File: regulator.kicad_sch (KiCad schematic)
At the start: 4 parts, among them U1 TEN20-4811WIN, U2 ADP7142AUJZ

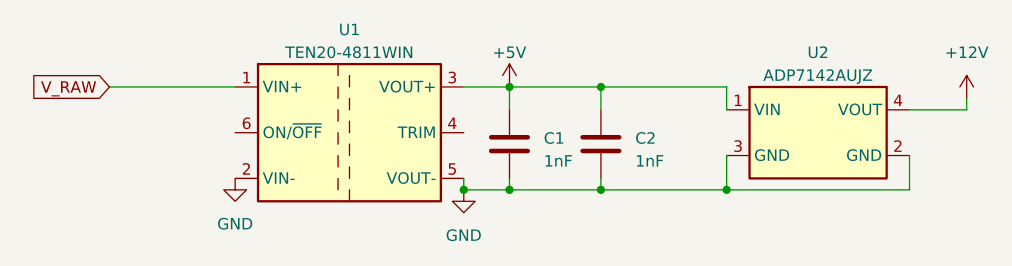
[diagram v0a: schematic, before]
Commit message: initial pcb placment, some components needs to be replaced by smd
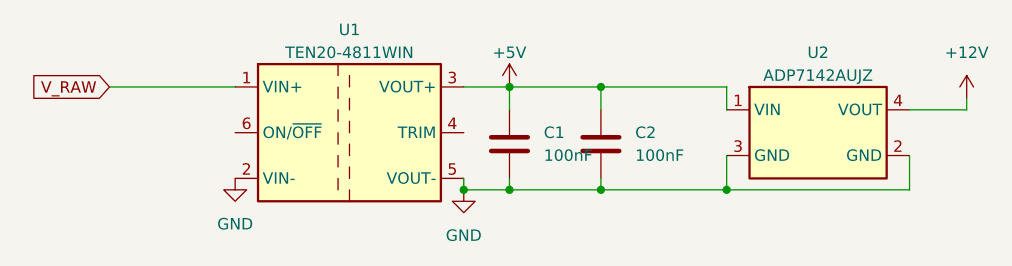
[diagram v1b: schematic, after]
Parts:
- C1, C2: value 1nF -> 100nF; footprint Capacitor_SMD:C_0805_2012Metric_Pad1.18x1.45mm_HandSolder -> Capacitor_THT:CP_Radial_Tantal_D5.5mm_P5.00mm
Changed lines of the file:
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@@
   (symbol (lib_id "Device:C") (at 142.24 92.71 180) (unit 1)
     (in_bom yes) (on_board yes) (dnp no) (fields_autoplaced)
-    (property "Reference" "C1" (at 146.05 92.075 0)
+    (property "Reference" "C1" (at 146.05 91.44 0)
       (effects (font (size 1.27 1.27)) (justify right))
     )
-    (property "Value" "1nF" (at 146.05 94.615 0)
+    (property "Value" "100nF" (at 146.05 93.98 0)
       (effects (font (size 1.27 1.27)) (justify right))
     )
-    (property "Footprint" "Capacitor_SMD:C_0805_2012Metric_Pad1.18x1.45mm_HandSolder" (at 141.2748 88.9 0)
+    (property "Footprint" "Capacitor_THT:CP_Radial_Tantal_D5.5mm_P5.00mm" (at 141.2748 88.9 0)
       (effects (font (size 1.27 1.27)) hide)
     )
@@
   (symbol (lib_id "Device:C") (at 152.4 92.71 180) (unit 1)
     (in_bom yes) (on_board yes) (dnp no) (fields_autoplaced)
-    (property "Reference" "C2" (at 156.21 92.075 0)
+    (property "Reference" "C2" (at 156.21 91.44 0)
       (effects (font (size 1.27 1.27)) (justify right))
     )
-    (property "Value" "1nF" (at 156.21 94.615 0)
+    (property "Value" "100nF" (at 156.21 93.98 0)
       (effects (font (size 1.27 1.27)) (justify right))
     )
-    (property "Footprint" "Capacitor_SMD:C_0805_2012Metric_Pad1.18x1.45mm_HandSolder" (at 151.4348 88.9 0)
+    (property "Footprint" "Capacitor_THT:CP_Radial_Tantal_D5.5mm_P5.00mm" (at 151.4348 88.9 0)
       (effects (font (size 1.27 1.27)) hide)
     )

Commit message: Added first pcb design
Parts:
- C1, C2: footprint Capacitor_THT:CP_Radial_Tantal_D5.5mm_P5.00mm -> Capacitor_SMD:C_0805_2012Metric_Pad1.18x1.45mm_HandSolder
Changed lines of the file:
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@@
       (effects (font (size 1.27 1.27)) (justify right))
     )
-    (property "Footprint" "Capacitor_THT:CP_Radial_Tantal_D5.5mm_P5.00mm" (at 141.2748 88.9 0)
+    (property "Footprint" "Capacitor_SMD:C_0805_2012Metric_Pad1.18x1.45mm_HandSolder" (at 141.2748 88.9 0)
       (effects (font (size 1.27 1.27)) hide)
     )
@@
       (effects (font (size 1.27 1.27)) (justify right))
     )
-    (property "Footprint" "Capacitor_THT:CP_Radial_Tantal_D5.5mm_P5.00mm" (at 151.4348 88.9 0)
+    (property "Footprint" "Capacitor_SMD:C_0805_2012Metric_Pad1.18x1.45mm_HandSolder" (at 151.4348 88.9 0)
       (effects (font (size 1.27 1.27)) hide)
     )
